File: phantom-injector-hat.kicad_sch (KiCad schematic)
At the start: 38 parts, among them J1 Conn_02x20_Odd_Even, J2 Conn_02x03_Top_Bottom, J3 Conn_01x03, J4 Conn_01x03, SW1 SW_SPST, SW2 SW_SPST, U1 LT8362EMSE-PBF

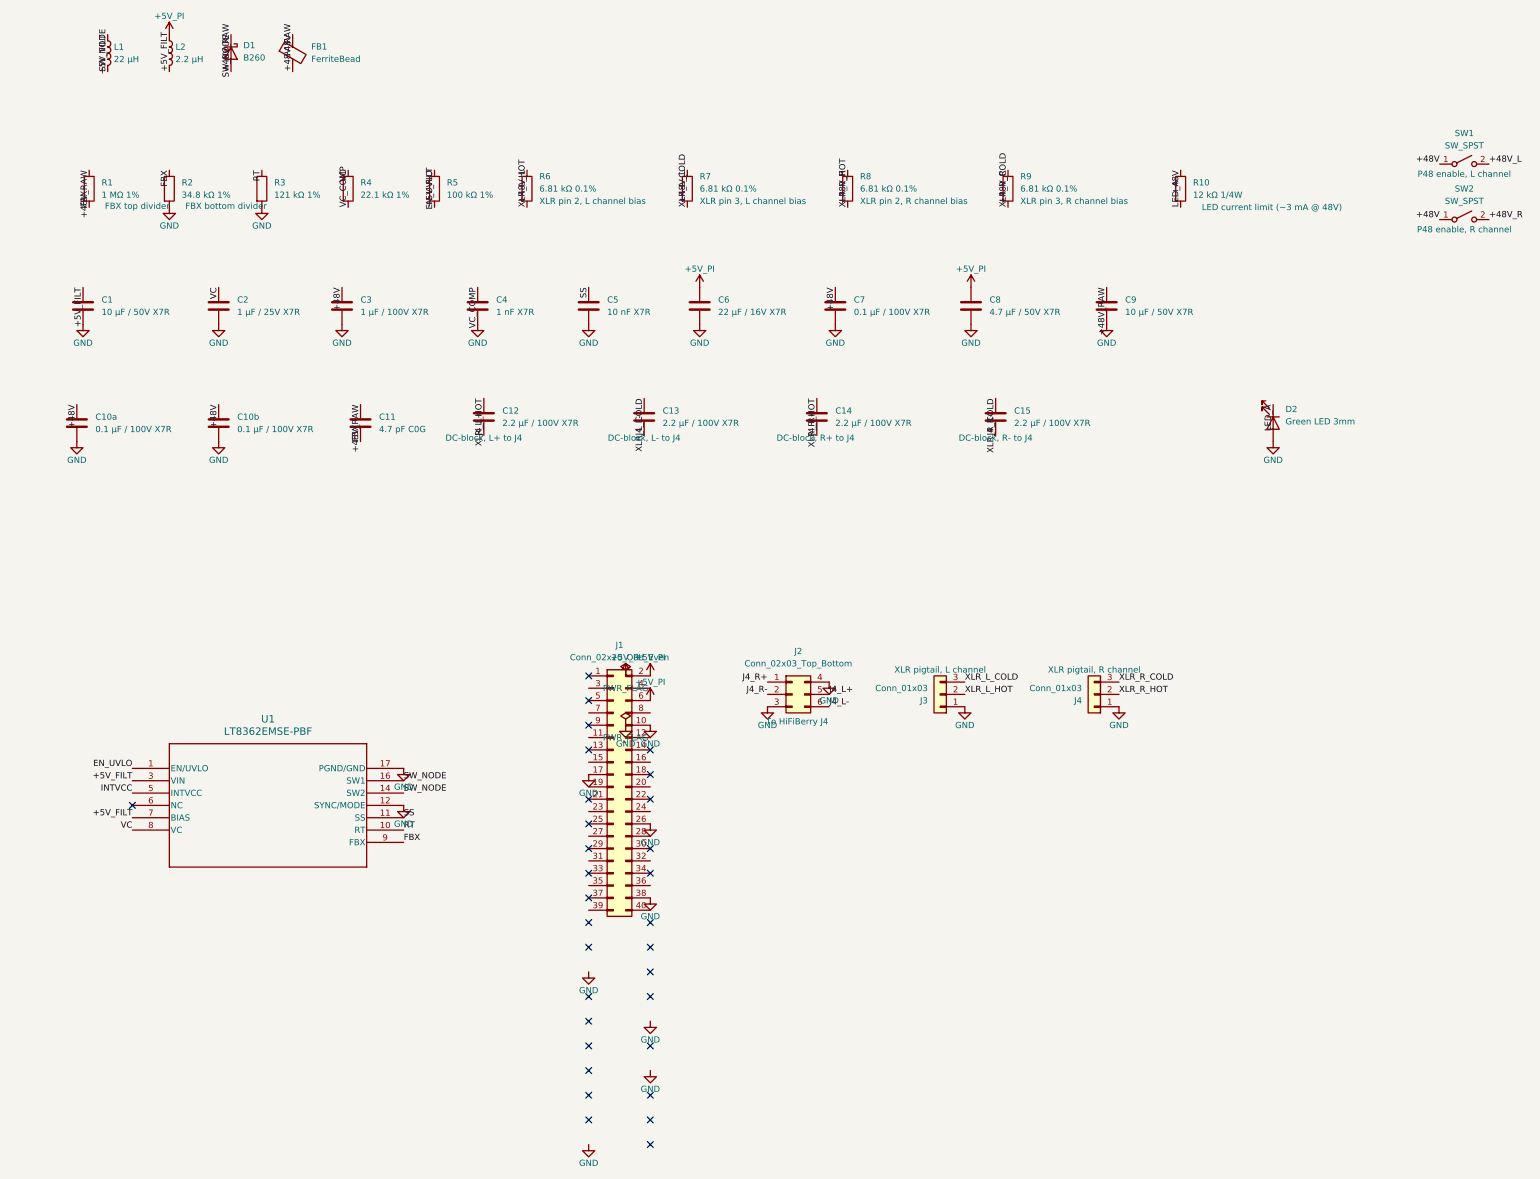
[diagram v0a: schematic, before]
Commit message: Add R11/C16, fix SYNC/MODE for Burst+SSFM, fix script idempotency
- Add R11 (100kΩ, 0805): SYNC/MODE pull-down to GND, selects Burst+SSFM
  mode per LT8362 datasheet (low EMI at load, low quiescent when idle)
- Add C16 (1µF/10V X7R, 0805): INTVCC bypass, required minimum per datasheet
  (INTVCC = 3.2V LDO; 1µF low ESR ceramic is mandatory, not optional)
- Fix U1 pin 12 (SYNC/MODE) net: was incorrectly tied to GND (Burst only),
  now on SYNC_MODE net driven by R11
- Fix wire_schematic.py block extraction: use explicit '\t' prefix instead of
  scanning back to line_start, preventing extra ')' accumulation on each run
- Verify V_FB = 1.60V from LT8362 datasheet (closes open item)
- ERC: 13 warnings, all expected (same as baseline)

Co-Authored-By: Claude Sonnet 4.6 <noreply@anthropic.com>
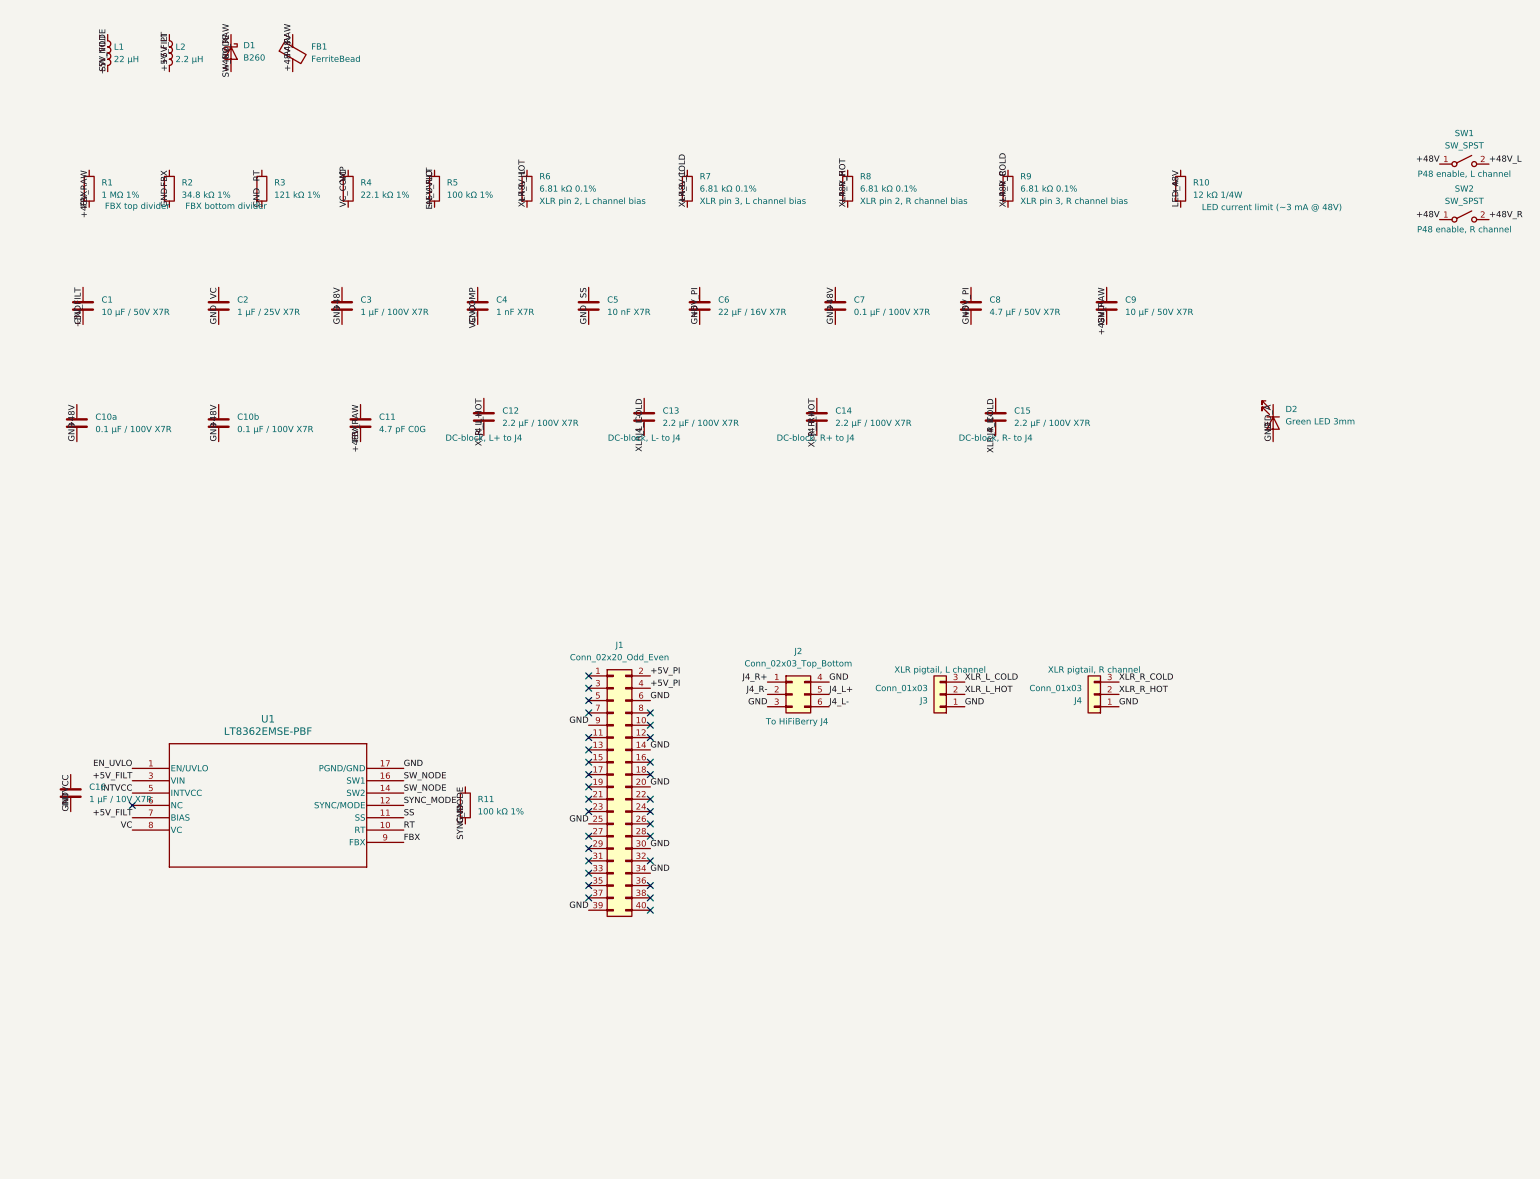
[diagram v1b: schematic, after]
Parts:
- added C16: 1 µF / 10V X7R, Capacitor_SMD:C_0805_2012Metric_Pad1.18x1.45mm_HandSolder, symbol Device:C
- added R11: 100 kΩ 1%, Resistor_SMD:R_0805_2012Metric_Pad1.20x1.40mm_HandSolder, symbol Device:R
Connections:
- net +5V_PI: now also J1.4 (Pin_4); no longer J1.6 (Pin_6)
- net INTVCC: now also C16.1
- net GND: now reaches C7.2
- net GND: now also C1.2, C10a.2, C10b.2, C2.2, C3.2, C4.2, C5.2, C6.2, C8.2, C9.2, D2.2 (A), J1.14 (Pin_14), J1.20 (Pin_20), J1.25 (Pin_25), J1.30 (Pin_30), J1.34 (Pin_34), J1.39 (Pin_39), J1.6 (Pin_6), J1.9 (Pin_9), J2.3 (Pin_3), J2.4 (Pin_4), J3.1 (Pin_1), J4.1 (Pin_1), R2.2, R3.2, U1.17 (PGND/GND), C16.2, R11.2
- net SYNC_MODE: now reaches U1.12 (SYNC/MODE)
- net SYNC_MODE: now also R11.1

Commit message: Add C17/C18, fix C10a/C10b annotation, register U1 footprint library
- Rename C10a→C10, C10b→C11, cascade C11-C17→C12-C18 (KiCad requires
  numeric-only suffixes; C10a/C10b caused ERC annotation errors)
- Add C18 (100nF 0805 X7R): BIAS pin local bypass per LT8362 datasheet
- Create fp-lib-table registering ul_LT8362EMSE-PBF via ${KIPRJMOD}-relative
  path; update U1 footprint to ul_LT8362EMSE-PBF:MSE_16A_ADI
- Add ERC.rpt (13 warnings, 0 errors — all expected pin_to_pin from
  unspecified LT8362 pin types + footprint_link_issues now resolved)
- Add lt8362.pdf datasheet

Co-Authored-By: Claude Sonnet 4.6 <noreply@anthropic.com>
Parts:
- added C18: 100 nF / 10V X7R, Capacitor_SMD:C_0805_2012Metric_Pad1.18x1.45mm_HandSolder, symbol Device:C
- U1: footprint MSE_16A_ADI -> ul_LT8362EMSE-PBF:MSE_16A_ADI
- renumbered C10a to C10, C10b to C11, C11 to C12, C12 to C13, C13 to C14, C14 to C15, C15 to C16, C16 to C17
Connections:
- net +5V_FILT: now also C18.1
- net GND: now also C18.2
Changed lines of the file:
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@@
+		)
+	)
+	(label "XLR_L_HOT"
+		(at 118.11 101.6 270)
+		(effects
+			(font
+				(size 1.27 1.27)
+			)
+			(justify right bottom)
+		)
+	)
+	(label "J4_L+"
+		(at 118.11 109.22 90)
+		(effects
+			(font
+				(size 1.27 1.27)
+			)
+			(justify left bottom)
+		)
+	)
+	(label "XLR_L_COLD"
+		(at 151.13 101.6 270)
+		(effects
+			(font
+				(size 1.27 1.27)
+			)
+			(justify right bottom)
+		)
+	)
+	(label "J4_L-"
+		(at 151.13 109.22 90)
+		(effects
+			(font
+				(size 1.27 1.27)
+			)
+			(justify left bottom)
+		)
+	)
+	(label "XLR_R_HOT"
+		(at 186.69 101.6 270)
+		(effects
+			(font
+				(size 1.27 1.27)
+			)
+			(justify right bottom)
+		)
+	)
+	(label "J4_R+"
+		(at 186.69 109.22 90)
+		(effects
+			(font
+				(size 1.27 1.27)
+			)
+			(justify left bottom)
+		)
+	)
+	(label "XLR_R_COLD"
+		(at 223.52 101.6 270)
+		(effects
+			(font
+				(size 1.27 1.27)
+			)
+			(justify right bottom)
+		)
+	)
+	(label "J4_R-"
+		(at 223.52 109.22 90)
+		(effects
+			(font
+				(size 1.27 1.27)
+			)
+			(justify left bottom)
 		)
 	)
@@
 		)
 	)
-	(label "XLR_L_HOT"
-		(at 118.11 101.6 270)
-		(effects
-			(font
-				(size 1.27 1.27)
-			)
-			(justify right bottom)
-		)
-	)
-	(label "J4_L+"
-		(at 118.11 109.22 90)
-		(effects
-			(font
-				(size 1.27 1.27)
-			)
-			(justify left bottom)
-		)
-	)
-	(label "XLR_L_COLD"
-		(at 151.13 101.6 270)
-		(effects
-			(font
-				(size 1.27 1.27)
-			)
-			(justify right bottom)
-		)
-	)
-	(label "J4_L-"
-		(at 151.13 109.22 90)
-		(effects
-			(font
-				(size 1.27 1.27)
-			)
-			(justify left bottom)
-		)
-	)
-	(label "XLR_R_HOT"
-		(at 186.69 101.6 270)
-		(effects
-			(font
-				(size 1.27 1.27)
-			)
-			(justify right bottom)
-		)
-	)
-	(label "J4_R+"
-		(at 186.69 109.22 90)
-		(effects
-			(font
-				(size 1.27 1.27)
-			)
-			(justify left bottom)
-		)
-	)
-	(label "XLR_R_COLD"
-		(at 223.52 101.6 270)
-		(effects
-			(font
-				(size 1.27 1.27)
-			)
-			(justify right bottom)
-		)
-	)
-	(label "J4_R-"
-		(at 223.52 109.22 90)
+	(label "+5V_FILT"
+		(at 22.86 184.15 270)
+		(effects
+			(font
+				(size 1.27 1.27)
+			)
+			(justify right bottom)
+		)
+	)
+	(label "GND"
+		(at 22.86 191.77 90)
 		(effects
 			(font
@@
 	)
 	(label "GND"
+		(at 152.4 173.99 0)
+		(effects
+			(font
+				(size 1.27 1.27)
+			)
+			(justify left bottom)
+		)
+	)
+	(label "GND"
+		(at 139.7 189.23 180)
+		(effects
+			(font
+				(size 1.27 1.27)
+			)
+			(justify right bottom)
+		)
+	)
+	(label "GND"
+		(at 152.4 199.39 0)
+		(effects
+			(font
+				(size 1.27 1.27)
+			)
+			(justify left bottom)
+		)
+	)
+	(label "GND"
+		(at 152.4 194.31 0)
+		(effects
+			(font
+				(size 1.27 1.27)
+			)
+			(justify left bottom)
+		)
+	)
+	(label "GND"
+		(at 152.4 163.83 0)
+		(effects
+			(font
+				(size 1.27 1.27)
+			)
+			(justify left bottom)
+		)
+	)
+	(label "GND"
+		(at 139.7 207.01 180)
+		(effects
+			(font
+				(size 1.27 1.27)
+			)
+			(justify right bottom)
+		)
+	)
+	(label "GND"
+		(at 139.7 168.91 180)
+		(effects
+			(font
+				(size 1.27 1.27)
+			)
+			(justify right bottom)
+		)
+	)
+	(label "GND"
 		(at 152.4 181.61 0)
-		(effects
-			(font
-				(size 1.27 1.27)
-			)
-			(justify left bottom)
-		)
-	)
-	(label "GND"
-		(at 139.7 189.23 180)
-		(effects
-			(font
-				(size 1.27 1.27)
-			)
-			(justify right bottom)
-		)
-	)
-	(label "GND"
-		(at 152.4 199.39 0)
-		(effects
-			(font
-				(size 1.27 1.27)
-			)
-			(justify left bottom)
-		)
-	)
-	(label "GND"
-		(at 139.7 168.91 180)
-		(effects
-			(font
-				(size 1.27 1.27)
-			)
-			(justify right bottom)
-		)
-	)
-	(label "GND"
-		(at 152.4 163.83 0)
-		(effects
-			(font
-				(size 1.27 1.27)
-			)
-			(justify left bottom)
-		)
-	)
-	(label "GND"
-		(at 139.7 207.01 180)
-		(effects
-			(font
-				(size 1.27 1.27)
-			)
-			(justify right bottom)
-		)
-	)
-	(label "GND"
-		(at 152.4 173.99 0)
-		(effects
-			(font
-				(size 1.27 1.27)
-			)
-			(justify left bottom)
-		)
-	)
-	(label "GND"
-		(at 152.4 194.31 0)
 		(effects
 			(font
@@
 	)
 	(no_connect (at 45.72 185.42))
+	(no_connect (at 139.7 196.85))
+	(no_connect (at 139.7 181.61))
+	(no_connect (at 139.7 201.93))
+	(no_connect (at 139.7 191.77))
+	(no_connect (at 152.4 186.69))
+	(no_connect (at 152.4 176.53))
+	(no_connect (at 139.7 204.47))
+	(no_connect (at 139.7 163.83))
+	(no_connect (at 139.7 199.39))
+	(no_connect (at 139.7 176.53))
+	(no_connect (at 152.4 191.77))
+	(no_connect (at 139.7 161.29))
+	(no_connect (at 139.7 184.15))
+	(no_connect (at 152.4 196.85))
+	(no_connect (at 152.4 179.07))
+	(no_connect (at 139.7 158.75))
+	(no_connect (at 152.4 207.01))
+	(no_connect (at 152.4 171.45))
+	(no_connect (at 152.4 201.93))
+	(no_connect (at 139.7 179.07))
+	(no_connect (at 139.7 186.69))
+	(no_connect (at 152.4 204.47))
+	(no_connect (at 139.7 173.99))
+	(no_connect (at 152.4 168.91))
+	(no_connect (at 152.4 189.23))
+	(no_connect (at 139.7 194.31))
 	(no_connect (at 139.7 171.45))
-	(no_connect (at 139.7 199.39))
+	(no_connect (at 152.4 166.37))
 	(no_connect (at 152.4 184.15))
-	(no_connect (at 139.7 176.53))
-	(no_connect (at 139.7 196.85))
 	(no_connect (at 139.7 166.37))
-	(no_connect (at 152.4 171.45))
-	(no_connect (at 139.7 158.75))
-	(no_connect (at 152.4 186.69))
-	(no_connect (at 152.4 207.01))
-	(no_connect (at 152.4 176.53))
-	(no_connect (at 139.7 191.77))
-	(no_connect (at 152.4 179.07))
-	(no_connect (at 139.7 179.07))
-	(no_connect (at 152.4 168.91))
-	(no_connect (at 139.7 186.69))
-	(no_connect (at 152.4 191.77))
-	(no_connect (at 152.4 196.85))
-	(no_connect (at 139.7 201.93))
-	(no_connect (at 152.4 189.23))
-	(no_connect (at 139.7 204.47))
-	(no_connect (at 139.7 161.29))
-	(no_connect (at 139.7 173.99))
-	(no_connect (at 139.7 163.83))
-	(no_connect (at 139.7 194.31))
-	(no_connect (at 152.4 166.37))
-	(no_connect (at 139.7 184.15))
-	(no_connect (at 152.4 204.47))
-	(no_connect (at 139.7 181.61))
-	(no_connect (at 152.4 201.93))
 )

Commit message: Assign correct footprints to SW1/SW2 and U1; add switch datasheet
SW1/SW2: replace placeholder footprints with
Button_Switch_THT:SW_Slide_SPDT_Angled_CK_OS102011MA1Q (standard KiCad
library, no fp-lib-table entry needed). Physical pad 3 will be unconnected
in DRC — expected, as the SPST symbol only drives pins 1 and 2.

U1: footprint already updated in prior commit; kicad_pro touched by KiCad.

Add Littelfuse-CK-Slide-OS-Series-Datasheet.pdf for reference.

Co-Authored-By: Claude Sonnet 4.6 <noreply@anthropic.com>
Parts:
- C3: footprint Capacitor_SMD:C_1206_3216Metric_Pad1.33x1.80mm_HandSolder -> Button_Switch_THT:SW_Slide_SPDT_Angled_CK_OS102011MA1Q
- J3, J4: footprint Connector_PinHeader_2.54mm:PinHeader_1x03_P2.54mm_Vertical_SMD_Pin1Left -> Button_Switch_THT:SW_Slide_SPDT_Angled_CK_OS102011MA1Q
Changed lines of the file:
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@@
+	)
+	(label "GND"
+		(at 152.4 194.31 0)
+		(effects
+			(font
+				(size 1.27 1.27)
+			)
+			(justify left bottom)
+		)
+	)
+	(label "GND"
+		(at 139.7 168.91 180)
+		(effects
+			(font
+				(size 1.27 1.27)
+			)
+			(justify right bottom)
+		)
+	)
+	(label "GND"
+		(at 152.4 163.83 0)
+		(effects
+			(font
+				(size 1.27 1.27)
+			)
+			(justify left bottom)
+		)
+	)
+	(label "GND"
+		(at 152.4 199.39 0)
+		(effects
+			(font
+				(size 1.27 1.27)
+			)
+			(justify left bottom)
+		)
+	)
+	(label "GND"
+		(at 139.7 207.01 180)
+		(effects
+			(font
+				(size 1.27 1.27)
+			)
+			(justify right bottom)
+		)
 	)
 	(label "GND"
@@
 	)
 	(label "GND"
-		(at 152.4 199.39 0)
+		(at 152.4 181.61 0)
 		(effects
 			(font
@@
 		)
 	)
-	(label "GND"
-		(at 152.4 194.31 0)
-		(effects
-			(font
-				(size 1.27 1.27)
-			)
-			(justify left bottom)
-		)
-	)
-	(label "GND"
-		(at 152.4 163.83 0)
-		(effects
-			(font
-				(size 1.27 1.27)
-			)
-			(justify left bottom)
-		)
-	)
-	(label "GND"
-		(at 139.7 207.01 180)
-		(effects
-			(font
-				(size 1.27 1.27)
-			)
-			(justify right bottom)
-		)
-	)
-	(label "GND"
-		(at 139.7 168.91 180)
-		(effects
-			(font
-				(size 1.27 1.27)
-			)
-			(justify right bottom)
-		)
-	)
-	(label "GND"
-		(at 152.4 181.61 0)
+	(label "+5V_PI"
+		(at 152.4 161.29 0)
 		(effects
 			(font
@@
 		)
 	)
-	(label "+5V_PI"
-		(at 152.4 161.29 0)
-		(effects
-			(font
-				(size 1.27 1.27)
-			)
-			(justify left bottom)
-		)
-	)
 	(no_connect (at 45.72 185.42))
+	(no_connect (at 152.4 184.15))
+	(no_connect (at 152.4 191.77))
+	(no_connect (at 139.7 181.61))
+	(no_connect (at 139.7 158.75))
+	(no_connect (at 139.7 199.39))
+	(no_connect (at 139.7 201.93))
+	(no_connect (at 139.7 176.53))
+	(no_connect (at 139.7 161.29))
+	(no_connect (at 139.7 186.69))
+	(no_connect (at 152.4 186.69))
+	(no_connect (at 139.7 194.31))
+	(no_connect (at 152.4 204.47))
+	(no_connect (at 152.4 166.37))
+	(no_connect (at 152.4 179.07))
+	(no_connect (at 152.4 189.23))
 	(no_connect (at 139.7 196.85))
-	(no_connect (at 139.7 181.61))
-	(no_connect (at 139.7 201.93))
+	(no_connect (at 152.4 176.53))
+	(no_connect (at 139.7 166.37))
+	(no_connect (at 139.7 163.83))
+	(no_connect (at 152.4 201.93))
+	(no_connect (at 139.7 171.45))
+	(no_connect (at 152.4 207.01))
+	(no_connect (at 139.7 204.47))
 	(no_connect (at 139.7 191.77))
-	(no_connect (at 152.4 186.69))
-	(no_connect (at 152.4 176.53))
-	(no_connect (at 139.7 204.47))
-	(no_connect (at 139.7 163.83))
-	(no_connect (at 139.7 199.39))
-	(no_connect (at 139.7 176.53))
-	(no_connect (at 152.4 191.77))
-	(no_connect (at 139.7 161.29))
+	(no_connect (at 152.4 196.85))
+	(no_connect (at 152.4 168.91))
 	(no_connect (at 139.7 184.15))
-	(no_connect (at 152.4 196.85))
-	(no_connect (at 152.4 179.07))
-	(no_connect (at 139.7 158.75))
-	(no_connect (at 152.4 207.01))
+	(no_connect (at 139.7 179.07))
+	(no_connect (at 139.7 173.99))
 	(no_connect (at 152.4 171.45))
-	(no_connect (at 152.4 201.93))
-	(no_connect (at 139.7 179.07))
-	(no_connect (at 139.7 186.69))
-	(no_connect (at 152.4 204.47))
-	(no_connect (at 139.7 173.99))
-	(no_connect (at 152.4 168.91))
-	(no_connect (at 152.4 189.23))
-	(no_connect (at 139.7 194.31))
-	(no_connect (at 139.7 171.45))
-	(no_connect (at 152.4 166.37))
-	(no_connect (at 152.4 184.15))
-	(no_connect (at 139.7 166.37))
 )
